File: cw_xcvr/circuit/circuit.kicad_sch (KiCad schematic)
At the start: 4 parts

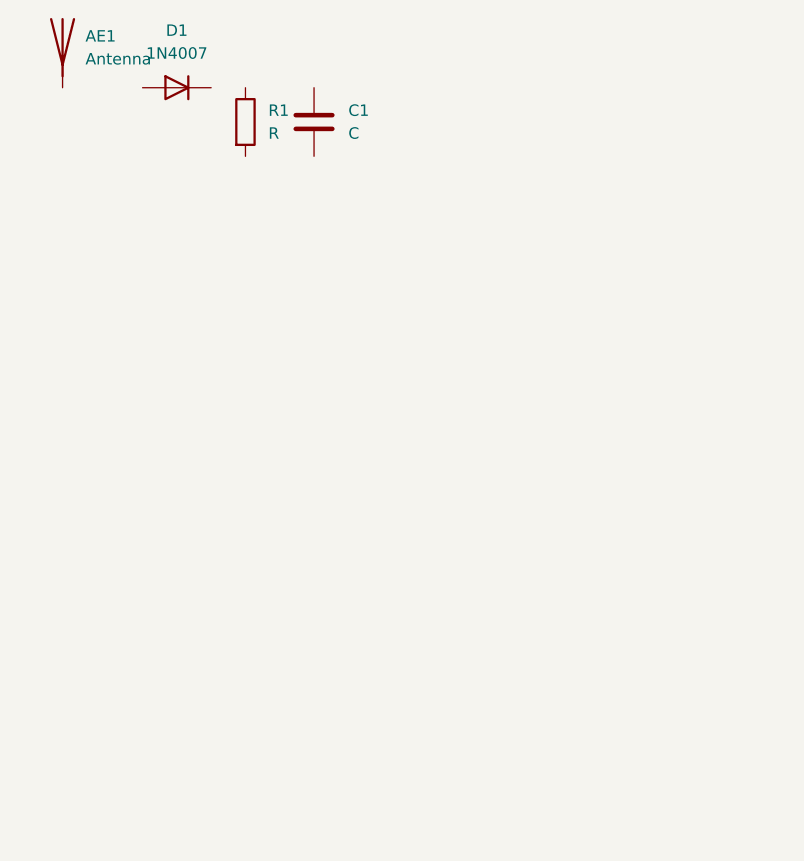
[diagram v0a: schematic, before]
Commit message: Buck converter simulation
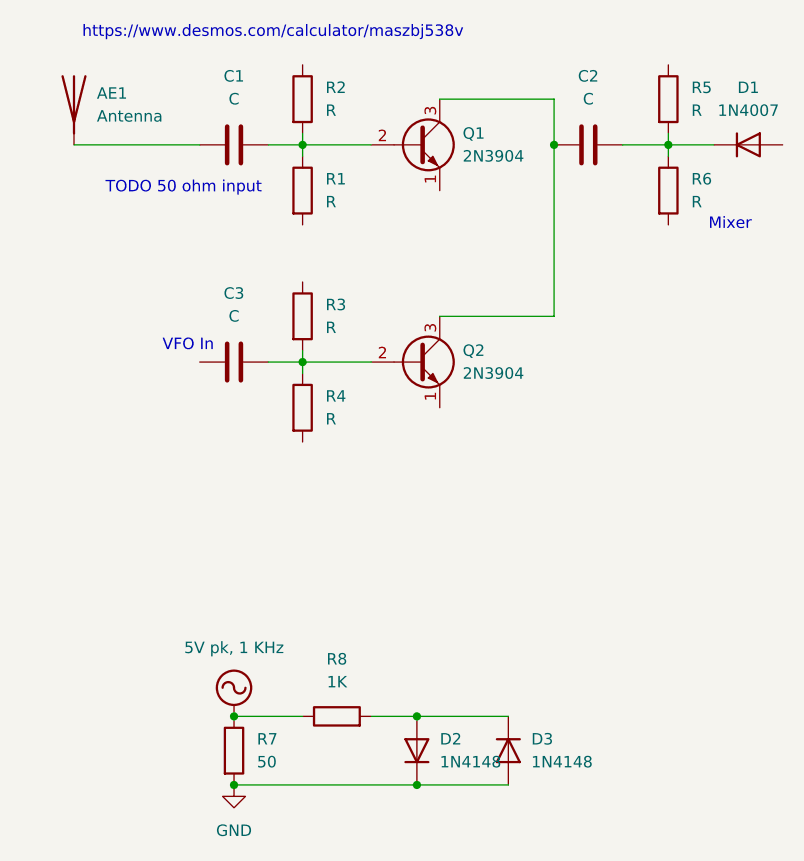
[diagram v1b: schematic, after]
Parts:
- added C2, C3: C, symbol Device:C
- added D2, D3: 1N4148, Diode_THT:D_DO-35_SOD27_P7.62mm_Horizontal, symbol Diode:1N4148
- added Q1, Q2: 2N3904, Package_TO_SOT_THT:TO-92_Inline, symbol Transistor_BJT:2N3904
- added R2, R3, R4, R5, R6: R, symbol Device:R
- added R7: 50, symbol Device:R
- added R8: 1K, symbol Device:R
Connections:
- net at D1.1 (K): now also C2.2, R5.2, R6.1
- net at AE1.1 (A): now also C1.1
- net at C1.2: now also R1.1, Q1.2 (B), R2.2
- new net: C3.2, Q2.2 (B), R3.2, R4.1
- new net: C2.1, Q1.3 (C), Q2.3 (C)
- new net: D2.2 (A), D3.1 (K), R8.2
- new net 5V pk, 1 KHz: R7.1, R8.1
- new net GND: D2.1 (K), D3.2 (A), R7.2
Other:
- note added: "Mixer"
- note added: "TODO 50 ohm input"
- note added: "VFO In"
- note added: "https://www.desmos.com/calculator/maszbj538v"
- moved on the sheet: AE1, C1, D1, R1
